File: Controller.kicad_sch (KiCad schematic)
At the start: 41 parts, among them J1 MOTOR0_PWM, J10 MOTOR3_PWR, J11 MOTOR4_PWR, J12 MOTOR5_PWR, J13 ARM0_ROT, J14 ARM0_GRB, J15 ARM1_ROT, J16 ARM1_GRB, J17 I2C1, J18 I2C1, J19 A0, J2 MOTOR1_PWM, J20 A1, J21 A2, J22 A3, J23 I2C2, J24 I2C2, J3 MOTOR2_PWM, J4 MOTOR3_PWM, J5 MOTOR4_PWM, J6 MOTOR5_PWM, J7 MOTOR0_PWR, J8 MOTOR1_PWR, J9 MOTOR2_PWR, U1 LM2576HVS-5, U2 LM2576HVS-3.3

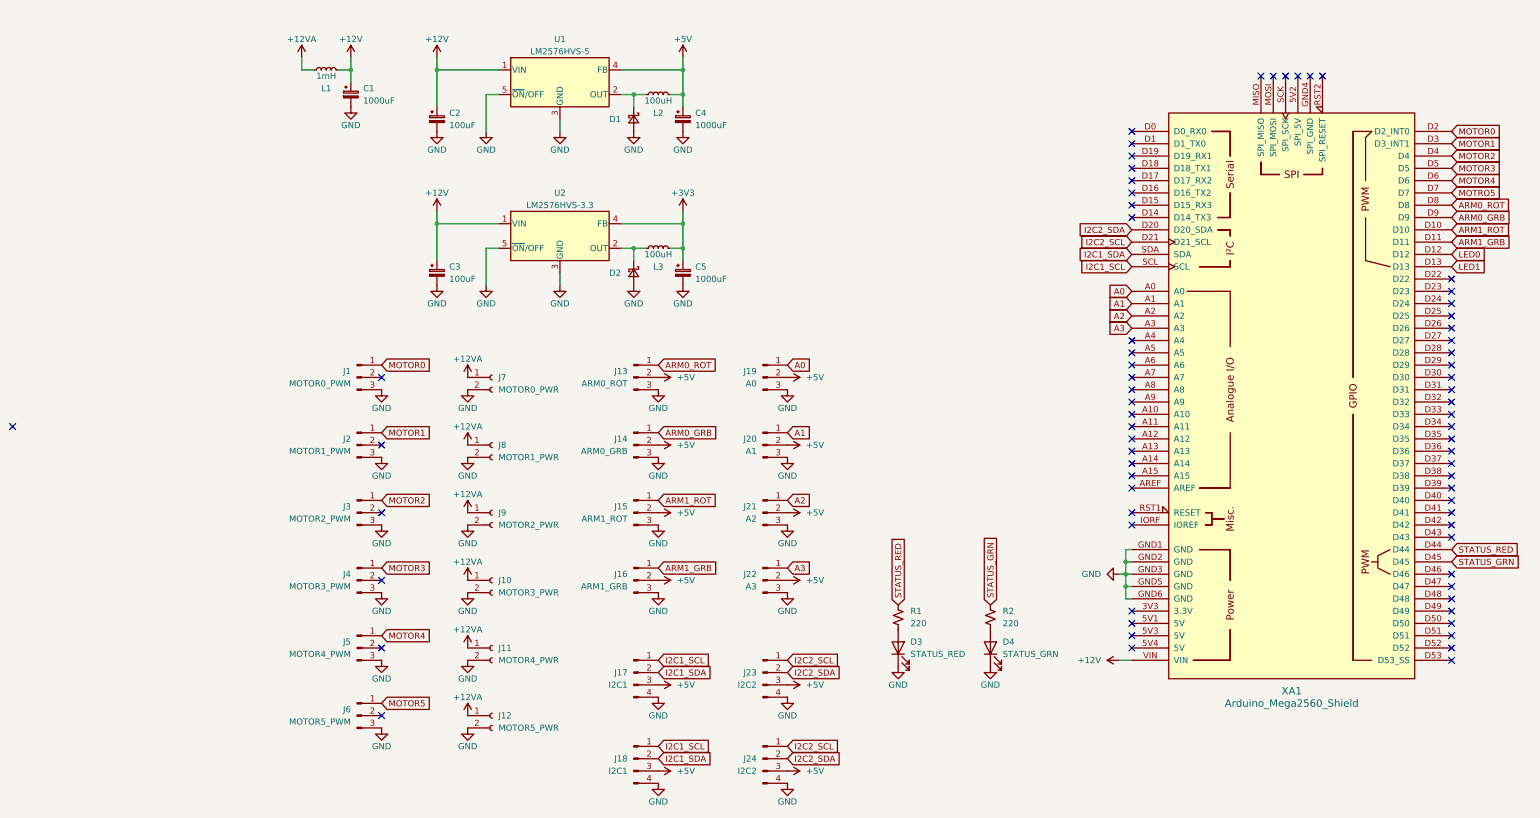
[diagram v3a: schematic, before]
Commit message: Update power supply
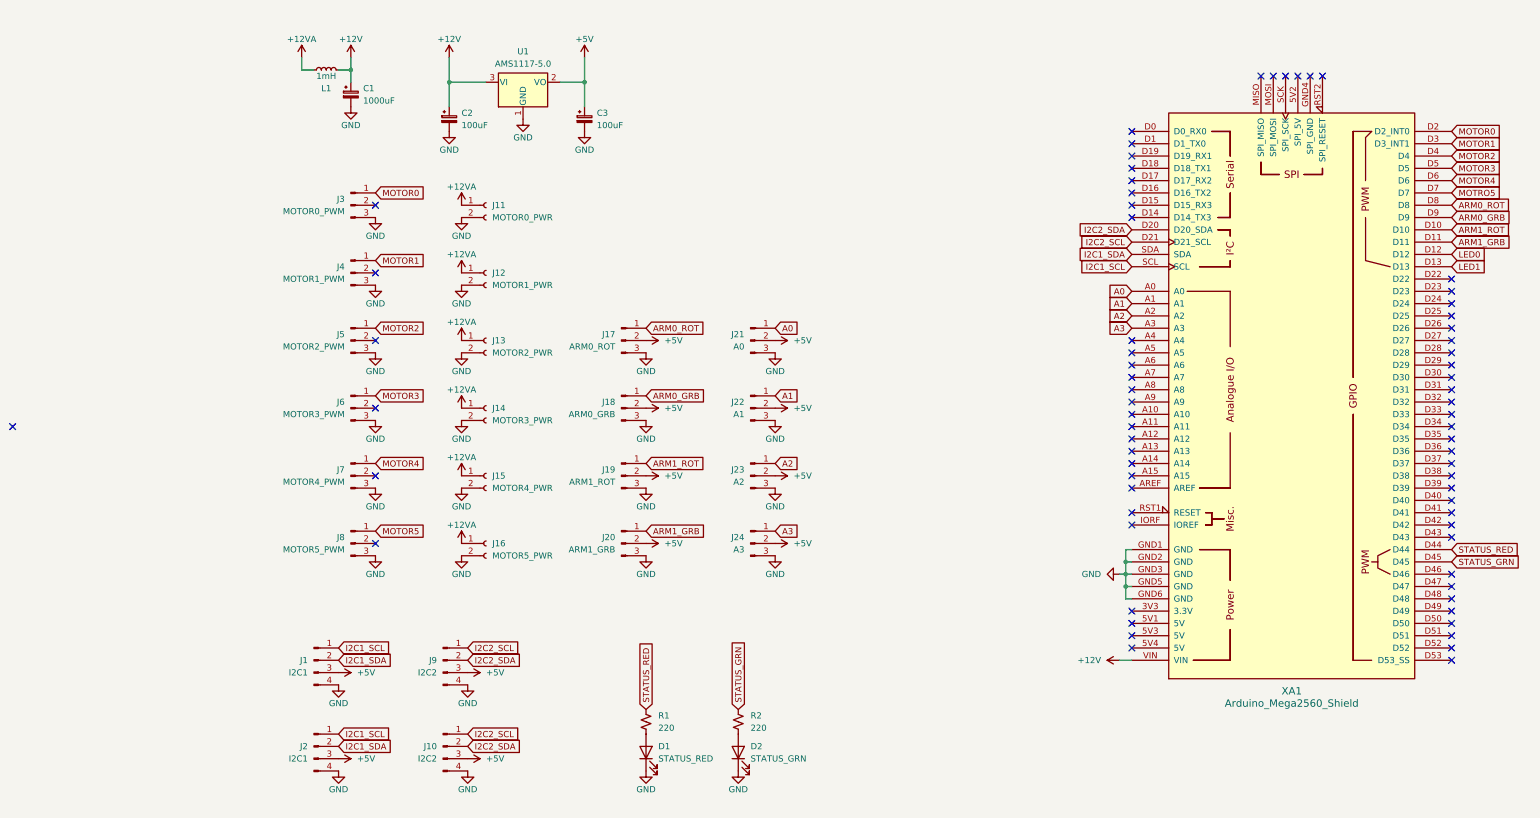
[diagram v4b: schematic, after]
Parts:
- removed C4, C5: 1000uF, Capacitor_THT:CP_Radial_D12.5mm_P5.00mm, symbol Device:C_Polarized_Small
- removed D1, D2: ~, Diode_SMD:D_SMC, symbol Device:D_Schottky_Small
- removed L2, L3: 100uH, Inductor_SMD:L_Bourns_SRR1210A, symbol Device:L_Small
- removed U1: LM2576HVS-5, Package_TO_SOT_SMD:TO-263-5_TabPin3, symbol Regulator_Switching:LM2576HVS-5
- removed U2: LM2576HVS-3.3, Package_TO_SOT_SMD:TO-263-5_TabPin3, symbol Regulator_Switching:LM2576HVS-3.3
- added U1: AMS1117-5.0, Package_TO_SOT_SMD:SOT-223-3_TabPin2, symbol Regulator_Linear:AMS1117-5.0
- renumbered D3 to D1, D4 to D2, J17 to J1, J24 to J10, J7 to J11, J8 to J12, J9 to J13, J10 to J14, J11 to J15, J12 to J16, J13 to J17, J14 to J18, J15 to J19, J18 to J2, J16 to J20, J19 to J21, J20 to J22, J21 to J23, J22 to J24, J1 to J3, J2 to J4, J3 to J5, J4 to J6, J5 to J7, J6 to J8, J23 to J9
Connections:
- net +12V: now also U1.3 (VI); no longer C3.1
- net +5V: now also C3.1, U1.2 (VO)
- net GND: now also U1.1 (GND)
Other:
- moved on the sheet: C2, D1, D2, J1, J10, J11, J12, J13, J14, J15, J16, J17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

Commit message: Complete full schematic
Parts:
- added J25: LED0, Controller:ESC-PWR, symbol Connector:Conn_01x02_Female
- added J26: LED1, Controller:ESC-PWR, symbol Connector:Conn_01x02_Female
- added Q1, Q2: FDB4030L, Package_TO_SOT_SMD:TO-263-2, symbol Device:Q_NMOS_GDS
- J1, J10, J2, J9: footprint Connector_PinHeader_2.54mm:PinHeader_1x04_P2.54mm_Vertical -> Connector_PinHeader_2.54mm:PinHeader_1x04_P2.54mm_Horizontal
- J17, J18, J19, J20, J21, J22, J23, J24: footprint Connector_PinHeader_2.54mm:PinHeader_1x03_P2.54mm_Vertical -> Connector_PinHeader_2.54mm:PinHeader_1x03_P2.54mm_Horizontal
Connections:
- net +12VA: now also J25.1 (Pin_1), J26.1 (Pin_1)
- net GND: now also Q1.3 (S), Q2.3 (S)
- net LED0: now also Q1.1 (G)
- net LED1: now also Q2.1 (G)
- new net: J25.2 (Pin_2), Q1.2 (D)
- new net: J26.2 (Pin_2), Q2.2 (D)

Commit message: Add PCB design, minor corrections on schematic
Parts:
- added J27: MAIN_PWR, Controller:ESC-PWR, symbol Connector:Conn_01x02_Female
- J25, J26: footprint Controller:ESC-PWR -> TerminalBlock:TerminalBlock_bornier-2_P5.08mm
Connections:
- net MOTRO5 is gone; now on net MOTOR5: XA1.D7
- net +12VA: now also J27.1 (Pin_1)
- net GND: now also J27.2 (Pin_2)
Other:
- moved on the sheet: C1, C2, C3, J25, J26, L1, Q1, Q2, U1

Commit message: Switch servos to 12V unfiltered rail
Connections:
- net +12VA: now also J17.2 (Pin_2), J18.2 (Pin_2), J19.2 (Pin_2), J20.2 (Pin_2)
- net +5V: no longer J17.2 (Pin_2), J18.2 (Pin_2), J19.2 (Pin_2), J20.2 (Pin_2)
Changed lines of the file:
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@@
+    (pin "1")
+  )
+  (symbol (lib_id "power:+12VA") (at 95.25 127 270) (unit 1)
+    (in_bom yes) (on_board yes)
+    (property "Reference" "#PWR041" (id 0) (at 91.44 127 0)
+      (effects (font (size 1.27 1.27)) hide)
+    )
+    (property "Value" "+12VA" (id 1) (at 99.06 127 90)
+      (effects (font (size 1.27 1.27)) (justify left))
+    )
+    (property "Footprint" "" (id 2) (at 95.25 127 0)
+      (effects (font (size 1.27 1.27)) hide)
+    )
+    (property "Datasheet" "" (id 3) (at 95.25 127 0)
+      (effects (font (size 1.27 1.27)) hide)
+    )
     (pin "1")
   )
@@
     (pin "2")
   )
+  (symbol (lib_id "power:+12VA") (at 95.25 113.03 270) (unit 1)
+    (in_bom yes) (on_board yes)
+    (property "Reference" "#PWR039" (id 0) (at 91.44 113.03 0)
+      (effects (font (size 1.27 1.27)) hide)
+    )
+    (property "Value" "+12VA" (id 1) (at 99.06 113.03 90)
+      (effects (font (size 1.27 1.27)) (justify left))
+    )
+    (property "Footprint" "" (id 2) (at 95.25 113.03 0)
+      (effects (font (size 1.27 1.27)) hide)
+    )
+    (property "Datasheet" "" (id 3) (at 95.25 113.03 0)
+      (effects (font (size 1.27 1.27)) hide)
+    )
+    (pin "1")
+  )
   (symbol (lib_id "power:+12VA") (at 57.15 113.03 0) (unit 1)
     (in_bom yes) (on_board yes)
@@
     (pin "1")
   )
-  (symbol (lib_id "power:+5V") (at 95.25 85.09 270) (unit 1)
-    (in_bom yes) (on_board yes)
-    (property "Reference" "#PWR035" (id 0) (at 91.44 85.09 0)
-      (effects (font (size 1.27 1.27)) hide)
-    )
-    (property "Value" "+5V" (id 1) (at 99.06 85.09 90)
-      (effects (font (size 1.27 1.27)) (justify left))
-    )
-    (property "Footprint" "" (id 2) (at 95.25 85.09 0)
-      (effects (font (size 1.27 1.27)) hide)
-    )
-    (property "Datasheet" "" (id 3) (at 95.25 85.09 0)
-      (effects (font (size 1.27 1.27)) hide)
-    )
-    (pin "1")
-  )
   (symbol (lib_id "Connector:Conn_01x03_Male") (at 116.84 113.03 0) (unit 1)
     (in_bom yes) (on_board yes)
@@
     (pin "2")
     (pin "3")
+  )
+  (symbol (lib_id "power:+12VA") (at 95.25 99.06 270) (unit 1)
+    (in_bom yes) (on_board yes)
+    (property "Reference" "#PWR037" (id 0) (at 91.44 99.06 0)
+      (effects (font (size 1.27 1.27)) hide)
+    )
+    (property "Value" "+12VA" (id 1) (at 99.06 99.06 90)
+      (effects (font (size 1.27 1.27)) (justify left))
+    )
+    (property "Footprint" "" (id 2) (at 95.25 99.06 0)
+      (effects (font (size 1.27 1.27)) hide)
+    )
+    (property "Datasheet" "" (id 3) (at 95.25 99.06 0)
+      (effects (font (size 1.27 1.27)) hide)
+    )
+    (pin "1")
   )
   (symbol (lib_id "power:+5V") (at 58.42 153.67 270) (unit 1)
@@
     (pin "1")
   )
-  (symbol (lib_id "power:+5V") (at 95.25 127 270) (unit 1)
-    (in_bom yes) (on_board yes)
-    (property "Reference" "#PWR041" (id 0) (at 91.44 127 0)
-      (effects (font (size 1.27 1.27)) hide)
-    )
-    (property "Value" "+5V" (id 1) (at 99.06 127 90)
-      (effects (font (size 1.27 1.27)) (justify left))
-    )
-    (property "Footprint" "" (id 2) (at 95.25 127 0)
-      (effects (font (size 1.27 1.27)) hide)
-    )
-    (property "Datasheet" "" (id 3) (at 95.25 127 0)
-      (effects (font (size 1.27 1.27)) hide)
-    )
-    (pin "1")
-  )
   (symbol (lib_id "Connector:Conn_01x03_Male") (at 116.84 127 0) (unit 1)
     (in_bom yes) (on_board yes)
@@
     (pin "1")
     (pin "2")
+  )
+  (symbol (lib_id "power:+12VA") (at 95.25 85.09 270) (unit 1)
+    (in_bom yes) (on_board yes)
+    (property "Reference" "#PWR035" (id 0) (at 91.44 85.09 0)
+      (effects (font (size 1.27 1.27)) hide)
+    )
+    (property "Value" "+12VA" (id 1) (at 99.06 85.09 90)
+      (effects (font (size 1.27 1.27)) (justify left))
+    )
+    (property "Footprint" "" (id 2) (at 95.25 85.09 0)
+      (effects (font (size 1.27 1.27)) hide)
+    )
+    (property "Datasheet" "" (id 3) (at 95.25 85.09 0)
+      (effects (font (size 1.27 1.27)) hide)
+    )
+    (pin "1")
   )
   (symbol (lib_id "power:+12VA") (at 57.15 57.15 0) (unit 1)
@@
     (pin "1")
   )
-  (symbol (lib_id "power:+5V") (at 95.25 99.06 270) (unit 1)
-    (in_bom yes) (on_board yes)
-    (property "Reference" "#PWR037" (id 0) (at 91.44 99.06 0)
-      (effects (font (size 1.27 1.27)) hide)
-    )
-    (property "Value" "+5V" (id 1) (at 99.06 99.06 90)
-      (effects (font (size 1.27 1.27)) (justify left))
-    )
-    (property "Footprint" "" (id 2) (at 95.25 99.06 0)
-      (effects (font (size 1.27 1.27)) hide)
-    )
-    (property "Datasheet" "" (id 3) (at 95.25 99.06 0)
-      (effects (font (size 1.27 1.27)) hide)
-    )
-    (pin "1")
-  )
   (symbol (lib_id "Connector:Conn_01x02_Female") (at 172.72 33.02 0) (unit 1)
     (in_bom yes) (on_board yes)
@@
     )
     (property "Datasheet" "" (id 3) (at 54.61 36.83 0)
-      (effects (font (size 1.27 1.27)) hide)
-    )
-    (pin "1")
-  )
-  (symbol (lib_id "power:+5V") (at 95.25 113.03 270) (unit 1)
-    (in_bom yes) (on_board yes)
-    (property "Reference" "#PWR039" (id 0) (at 91.44 113.03 0)
-      (effects (font (size 1.27 1.27)) hide)
-    )
-    (property "Value" "+5V" (id 1) (at 99.06 113.03 90)
-      (effects (font (size 1.27 1.27)) (justify left))
-    )
-    (property "Footprint" "" (id 2) (at 95.25 113.03 0)
-      (effects (font (size 1.27 1.27)) hide)
-    )
-    (property "Datasheet" "" (id 3) (at 95.25 113.03 0)
       (effects (font (size 1.27 1.27)) hide)
     )
@@
       (reference "#PWR034") (unit 1) (value "GND") (footprint "")
     )
-    (path "/5d701a5b-35ab-4851-8ef2-ed4cd7ae2a3f"
-      (reference "#PWR035") (unit 1) (value "+5V") (footprint "")
+    (path "/9a51fda4-8aea-4149-9d95-6fd6132cdf25"
+      (reference "#PWR035") (unit 1) (value "+12VA") (footprint "")
     )
     (path "/a9696e43-3f81-4aa9-901f-150c6a0da3d7"
       (reference "#PWR036") (unit 1) (value "GND") (footprint "")
     )
-    (path "/d78fa016-64d3-4f57-99aa-64f0a9e5ca55"
-      (reference "#PWR037") (unit 1) (value "+5V") (footprint "")
+    (path "/61c10432-5892-4d1b-a56a-b39cde54c56d"
+      (reference "#PWR037") (unit 1) (value "+12VA") (footprint "")
     )
     (path "/7ef6b4b4-5840-405b-bf96-cdb17a805b7c"
       (reference "#PWR038") (unit 1) (value "GND") (footprint "")
     )
-    (path "/faa5c36d-42f5-4a0d-9691-1ba6c7a52fb6"
-      (reference "#PWR039") (unit 1) (value "+5V") (footprint "")
+    (path "/43777bed-4576-4aa7-84c2-7d4986523003"
+      (reference "#PWR039") (unit 1) (value "+12VA") (footprint "")
     )
     (path "/53d97fc1-e5e0-49e4-b136-d752f7560f2f"
       (reference "#PWR040") (unit 1) (value "GND") (footprint "")
     )
-    (path "/96854bfe-cf6e-43b1-913a-2c04114d38cf"
-      (reference "#PWR041") (unit 1) (value "+5V") (footprint "")
+    (path "/345483c9-aec0-4be0-ab14-092be6d8662f"
+      (reference "#PWR041") (unit 1) (value "+12VA") (footprint "")
     )
     (path "/71401763-c4ff-44c3-961e-3c2fdf52ec2d"

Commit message: Use 0603 resistors and LED
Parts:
- D1, D2: footprint Diode_SMD:D_0402_1005Metric -> Diode_SMD:D_0603_1608Metric_Pad1.05x0.95mm_HandSolder
- R1, R2: footprint Resistor_SMD:R_0402_1005Metric -> Resistor_SMD:R_0603_1608Metric_Pad0.98x0.95mm_HandSolder
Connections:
- net STATUS_GRN: now also R2.2; no longer R2.1
- net STATUS_RED: now also R1.2; no longer R1.1
- net at D1.2 (A): now also R1.1; no longer R1.2
- net at D2.2 (A): now also R2.1; no longer R2.2
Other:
- moved on the sheet: R1, R2
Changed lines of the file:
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@@
       (effects (font (size 1.27 1.27)) (justify right))
     )
-    (property "Footprint" "Diode_SMD:D_0402_1005Metric" (id 2) (at 95.25 170.18 0)
+    (property "Footprint" "Diode_SMD:D_0603_1608Metric_Pad1.05x0.95mm_HandSolder" (id 2) (at 95.25 170.18 0)
       (effects (font (size 1.27 1.27)) hide)
     )
@@
       (effects (font (size 1.27 1.27)) (justify right))
     )
-    (property "Footprint" "Diode_SMD:D_0402_1005Metric" (id 2) (at 114.3 170.18 0)
+    (property "Footprint" "Diode_SMD:D_0603_1608Metric_Pad1.05x0.95mm_HandSolder" (id 2) (at 114.3 170.18 0)
       (effects (font (size 1.27 1.27)) hide)
     )
@@
     (pin "3")
   )
-  (symbol (lib_id "Device:R_Small_US") (at 114.3 163.83 0) (unit 1)
-    (in_bom yes) (on_board yes)
-    (property "Reference" "R2" (id 0) (at 116.84 162.56 0)
-      (effects (font (size 1.27 1.27)) (justify left))
-    )
-    (property "Value" "220" (id 1) (at 116.84 165.1 0)
-      (effects (font (size 1.27 1.27)) (justify left))
-    )
-    (property "Footprint" "Resistor_SMD:R_0402_1005Metric" (id 2) (at 114.3 163.83 0)
+  (symbol (lib_id "Device:R_Small_US") (at 114.3 163.83 180) (unit 1)
+    (in_bom yes) (on_board yes)
+    (property "Reference" "R2" (id 0) (at 111.76 165.1 0)
+      (effects (font (size 1.27 1.27)) (justify left))
+    )
+    (property "Value" "220" (id 1) (at 111.76 162.56 0)
+      (effects (font (size 1.27 1.27)) (justify left))
+    )
+    (property "Footprint" "Resistor_SMD:R_0603_1608Metric_Pad0.98x0.95mm_HandSolder" (id 2) (at 114.3 163.83 0)
       (effects (font (size 1.27 1.27)) hide)
     )
@@
     (pin "2")
   )
-  (symbol (lib_id "Device:R_Small_US") (at 95.25 163.83 0) (unit 1)
-    (in_bom yes) (on_board yes)
-    (property "Reference" "R1" (id 0) (at 97.79 162.56 0)
-      (effects (font (size 1.27 1.27)) (justify left))
-    )
-    (property "Value" "220" (id 1) (at 97.79 165.1 0)
-      (effects (font (size 1.27 1.27)) (justify left))
-    )
-    (property "Footprint" "Resistor_SMD:R_0402_1005Metric" (id 2) (at 95.25 163.83 0)
+  (symbol (lib_id "Device:R_Small_US") (at 95.25 163.83 180) (unit 1)
+    (in_bom yes) (on_board yes)
+    (property "Reference" "R1" (id 0) (at 92.71 165.1 0)
+      (effects (font (size 1.27 1.27)) (justify left))
+    )
+    (property "Value" "220" (id 1) (at 92.71 162.56 0)
+      (effects (font (size 1.27 1.27)) (justify left))
+    )
+    (property "Footprint" "Resistor_SMD:R_0603_1608Metric_Pad0.98x0.95mm_HandSolder" (id 2) (at 95.25 163.83 0)
       (effects (font (size 1.27 1.27)) hide)
     )
@@
     )
     (path "/224848e5-7435-4a65-b58c-61159b27570c"
-      (reference "D1") (unit 1) (value "STATUS_RED") (footprint "Diode_SMD:D_0402_1005Metric")
+      (reference "D1") (unit 1) (value "STATUS_RED") (footprint "Diode_SMD:D_0603_1608Metric_Pad1.05x0.95mm_HandSolder")
     )
     (path "/2830c634-108b-46ef-9c05-c6ae96c053ac"
-      (reference "D2") (unit 1) (value "STATUS_GRN") (footprint "Diode_SMD:D_0402_1005Metric")
+      (reference "D2") (unit 1) (value "STATUS_GRN") (footprint "Diode_SMD:D_0603_1608Metric_Pad1.05x0.95mm_HandSolder")
     )
     (path "/f4618723-5941-418d-b6da-edc07bef531b"
@@
     )
     (path "/ebc4a2d8-81f7-47e5-a61b-37debe7e1d80"
-      (reference "R1") (unit 1) (value "220") (footprint "Resistor_SMD:R_0402_1005Metric")
+      (reference "R1") (unit 1) (value "220") (footprint "Resistor_SMD:R_0603_1608Metric_Pad0.98x0.95mm_HandSolder")
     )
     (path "/5af6305f-544d-4905-acdb-614e8bb9d366"
-      (reference "R2") (unit 1) (value "220") (footprint "Resistor_SMD:R_0402_1005Metric")
+      (reference "R2") (unit 1) (value "220") (footprint "Resistor_SMD:R_0603_1608Metric_Pad0.98x0.95mm_HandSolder")
     )
     (path "/abfff7e4-4e89-4e2d-816e-624233b98cb4"
